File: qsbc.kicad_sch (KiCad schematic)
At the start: 4 parts

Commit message: add inital ddr tool version, lots of routing work
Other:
- sheet DDR ports: added VDD_DRAM_1.2V; removed NVCC_DRAM_1.2V
- sheet Power ports: added NVCC_SNVS_1.8, VDD_DRAM_1.2V; removed NVCC_DRAM_1.2V, NVCC_SNVS_1P8
- sheet i.MX8MM Power ports: added VDD_DRAM_1.2V; removed NVCC_DRAM_1.2V

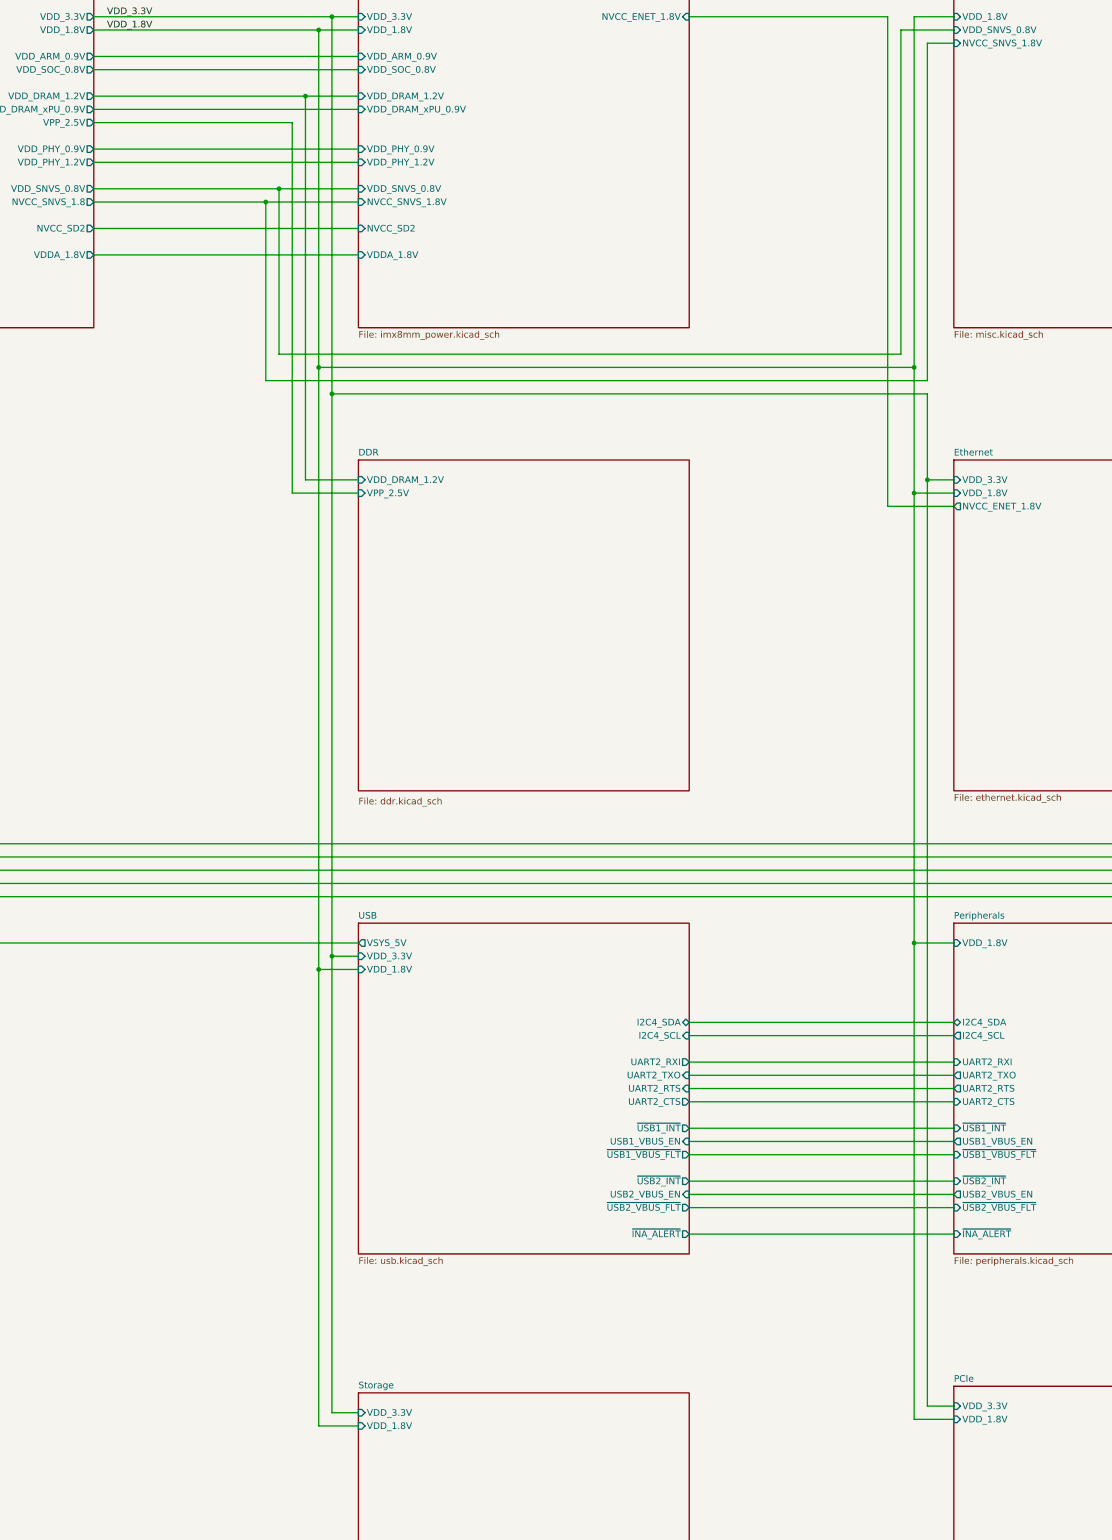
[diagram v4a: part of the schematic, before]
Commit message: more routing work, prepare to change to x32 lpddr4
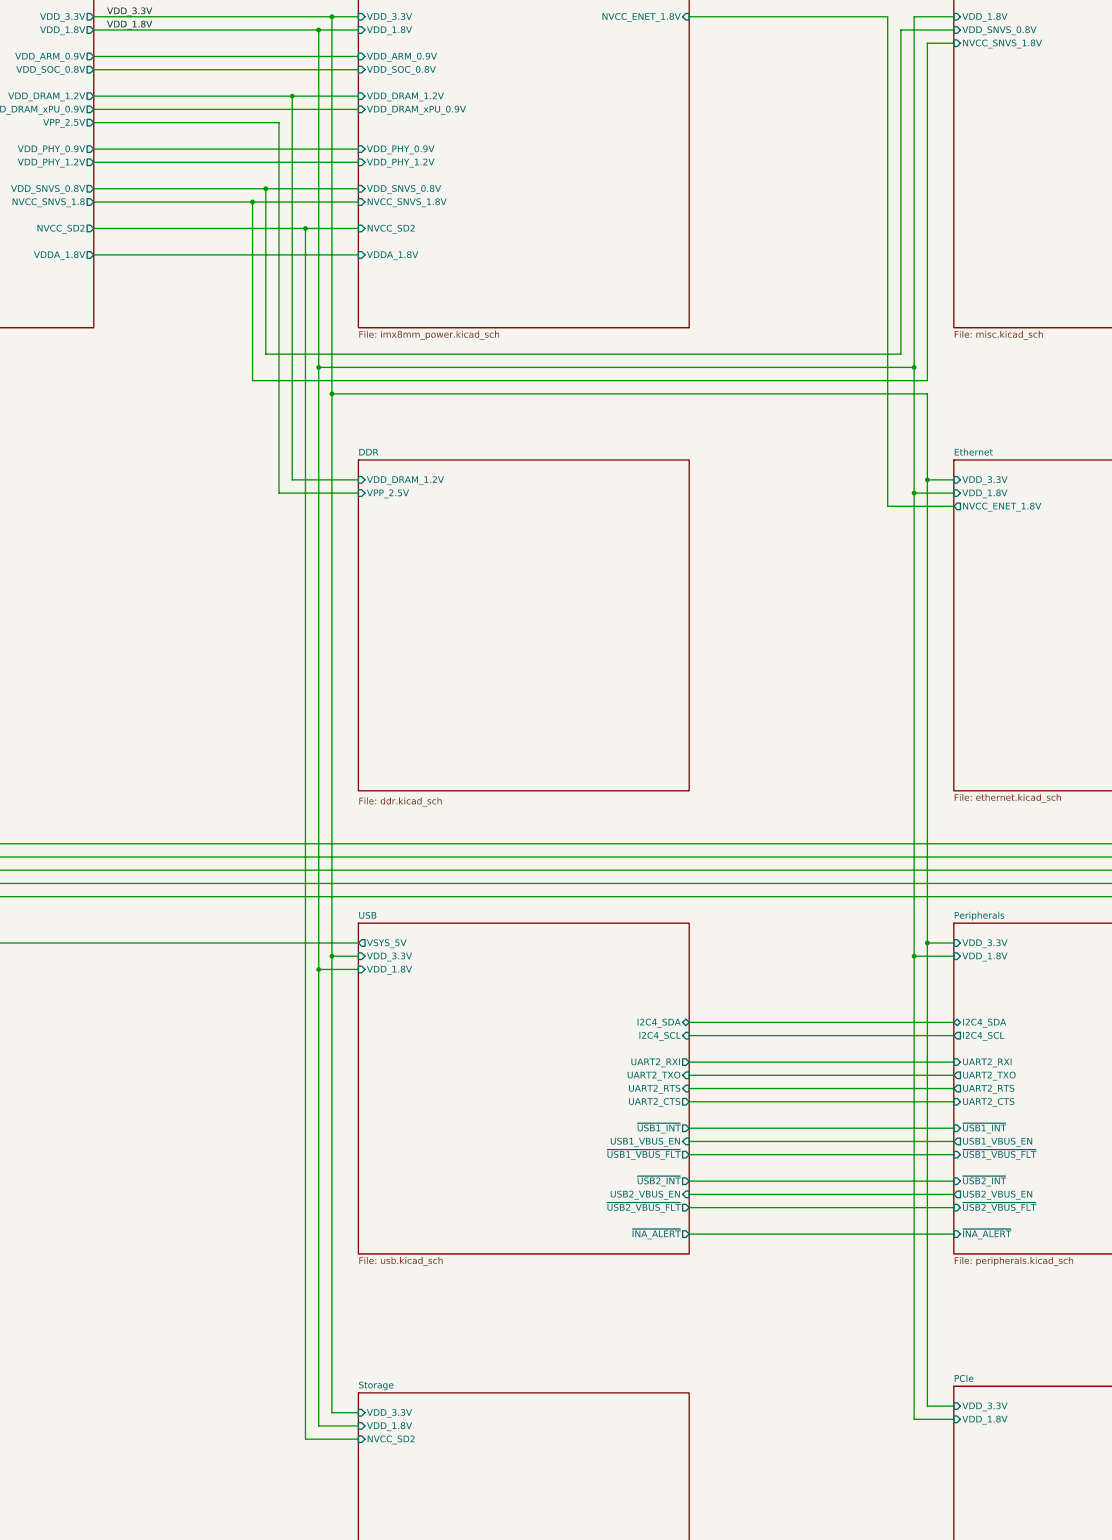
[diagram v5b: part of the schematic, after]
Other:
- sheet Peripherals ports: added VDD_3.3V; removed none
- sheet Storage ports: added NVCC_SD2; removed none

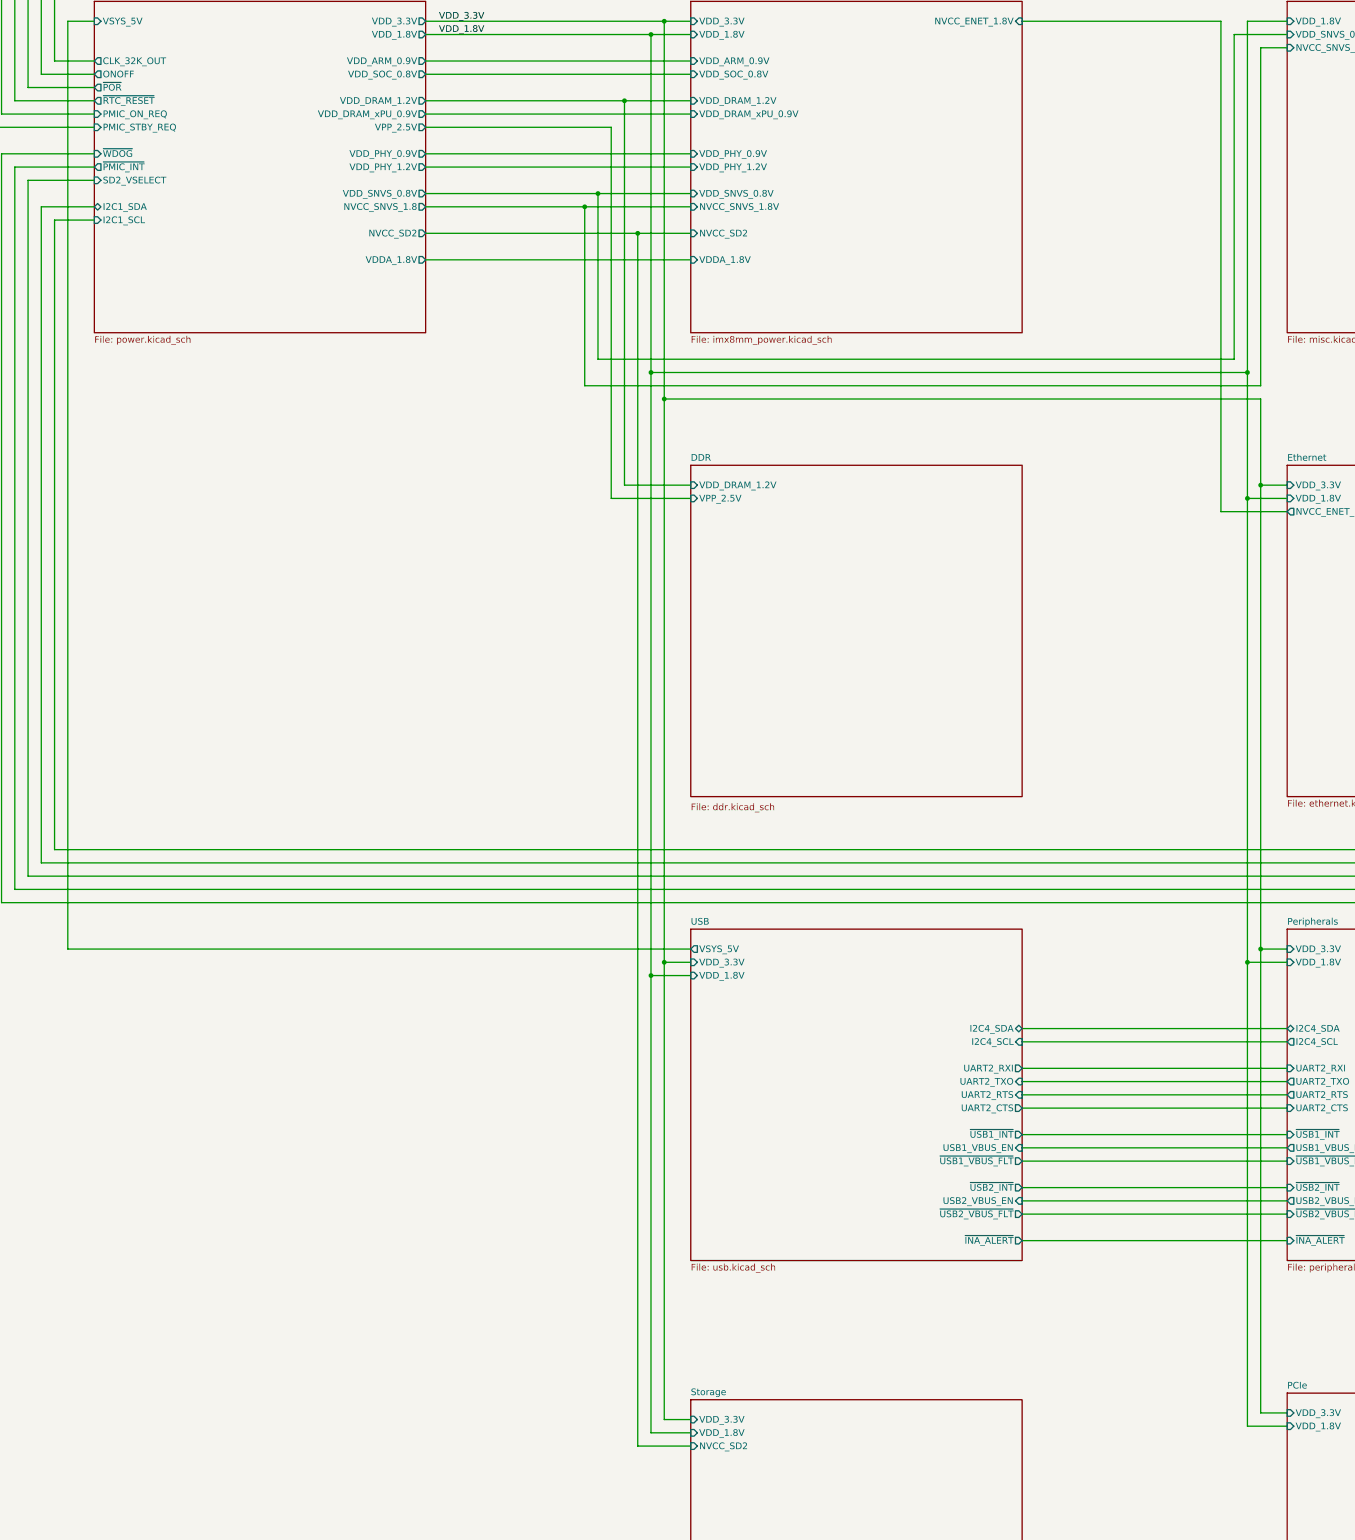
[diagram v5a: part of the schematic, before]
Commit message: inital routing of ddr data bus, sch work
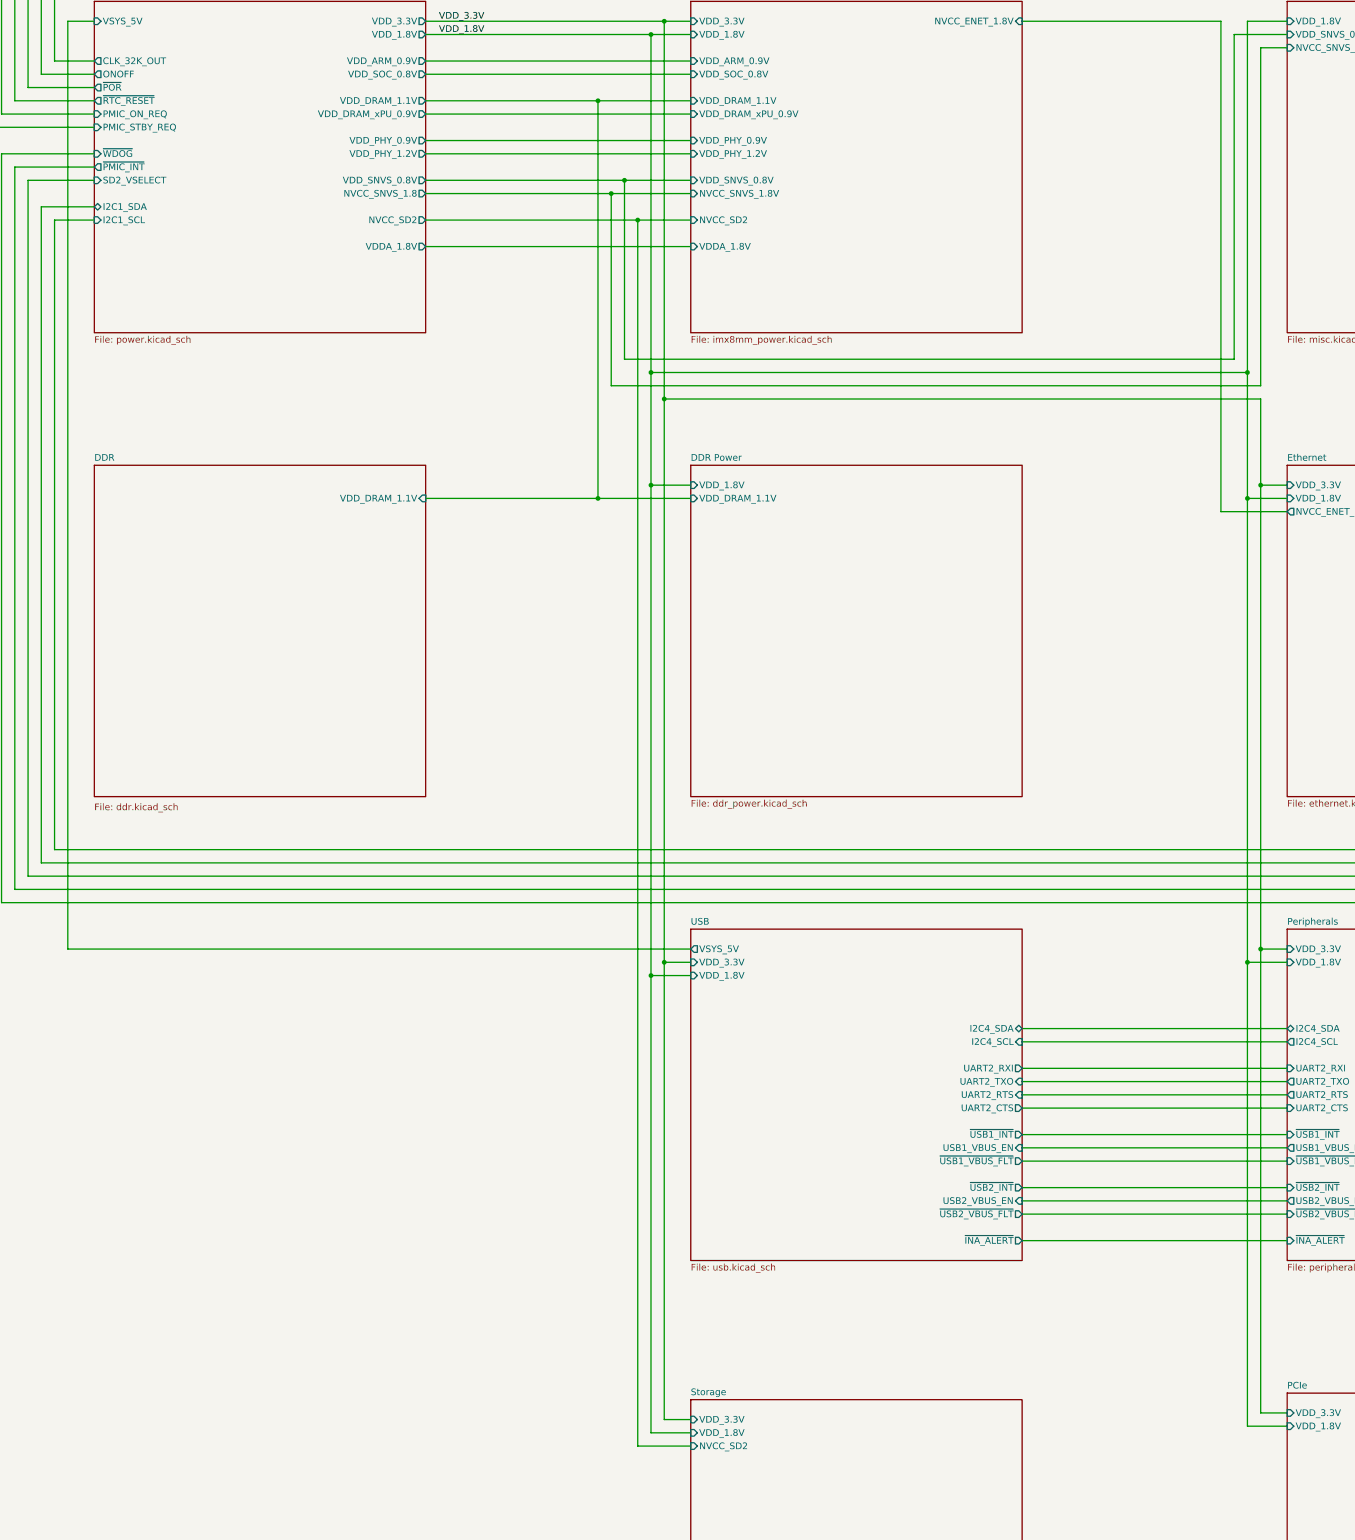
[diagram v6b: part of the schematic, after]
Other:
- added sheet DDR Power (ddr_power.kicad_sch)
- sheet DDR ports: added VDD_DRAM_1.1V; removed VDD_DRAM_1.2V, VPP_2.5V
- sheet Power ports: added VDD_DRAM_1.1V; removed VDD_DRAM_1.2V, VPP_2.5V
- sheet i.MX8MM Power ports: added VDD_DRAM_1.1V; removed VDD_DRAM_1.2V

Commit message: add SN65DSI86 DSI2DP ic, SCH, PCB work, flytime work
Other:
- added sheet Displayport (displayport.kicad_sch)
- sheet Peripherals ports: added DSI86_INT, ~{DSI86_EN}; removed none
